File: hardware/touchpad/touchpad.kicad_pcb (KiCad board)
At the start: 2 copper layers, 195.4 x 135.6 mm, 187 parts, among them J1 Conn_01x26_MountingPin, J10 Conn_02x03_Odd_Even, J100 Conn_02x03_Odd_Even, J101 Conn_02x03_Odd_Even, J102 Conn_02x03_Odd_Even, J103 Conn_02x03_Odd_Even, J104 Conn_02x03_Odd_Even, J105 Conn_02x03_Odd_Even, J106 Conn_02x03_Odd_Even, J107 Conn_02x03_Odd_Even, J108 Conn_02x03_Odd_Even, J109 Conn_02x03_Odd_Even, J11 Conn_02x03_Odd_Even, J110 Conn_02x03_Odd_Even, J111 Conn_02x03_Odd_Even, J112 Conn_02x03_Odd_Even, J113 Conn_02x03_Odd_Even, J114 Conn_02x03_Odd_Even, J115 Conn_02x03_Odd_Even, J116 Conn_02x03_Odd_Even, J117 Conn_02x03_Odd_Even, J118 Conn_02x03_Odd_Even, J119 Conn_02x03_Odd_Even, J12 Conn_02x03_Odd_Even, J120 Conn_02x03_Odd_Even, J121 Conn_02x03_Odd_Even, J122 Conn_02x03_Odd_Even, J123 Conn_02x03_Odd_Even, J124 Conn_02x03_Odd_Even, J125 Conn_02x03_Odd_Even, J126 Conn_02x03_Odd_Even, J127 Conn_02x03_Odd_Even, J128 Conn_02x03_Odd_Even, J129 Conn_02x03_Odd_Even, J13 Conn_02x03_Odd_Even, J130 Conn_02x03_Odd_Even, J131 Conn_02x03_Odd_Even, J132 Conn_02x03_Odd_Even, J133 Conn_02x03_Odd_Even, J134 Conn_02x03_Odd_Even, J135 Conn_02x03_Odd_Even, J136 Conn_02x03_Odd_Even, J137 Conn_02x03_Odd_Even, J138 Conn_02x03_Odd_Even, J139 Conn_02x03_Odd_Even, J14 Conn_02x03_Odd_Even, J140 Conn_02x03_Odd_Even, J141 Conn_02x03_Odd_Even, J142 Conn_02x03_Odd_Even, J143 Conn_02x03_Odd_Even, J144 Conn_02x03_Odd_Even, J145 Conn_02x03_Odd_Even, J146 Conn_02x03_Odd_Even, J147 Conn_02x03_Odd_Even, J148 Conn_02x03_Odd_Even, J149 Conn_02x03_Odd_Even, J15 Conn_02x03_Odd_Even, J150 Conn_02x03_Odd_Even, J151 Conn_02x03_Odd_Even, J152 Conn_02x03_Odd_Even, J153 Conn_02x03_Odd_Even, J154 Conn_02x03_Odd_Even, J155 Conn_02x03_Odd_Even, J156 Conn_02x03_Odd_Even, J157 Conn_02x03_Odd_Even, J158 Conn_02x03_Odd_Even, J159 Conn_02x03_Odd_Even, J16 Conn_02x03_Odd_Even, J160 Conn_02x03_Odd_Even, J161 Conn_02x03_Odd_Even, J162 Conn_02x03_Odd_Even, J163 Conn_02x03_Odd_Even, J164 Conn_02x03_Odd_Even, J165 Conn_02x03_Odd_Even, J166 Conn_02x03_Odd_Even, J167 Conn_02x03_Odd_Even, J168 Conn_02x03_Odd_Even, J169 Conn_02x03_Odd_Even, J17 Conn_02x03_Odd_Even, J170 Conn_02x03_Odd_Even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

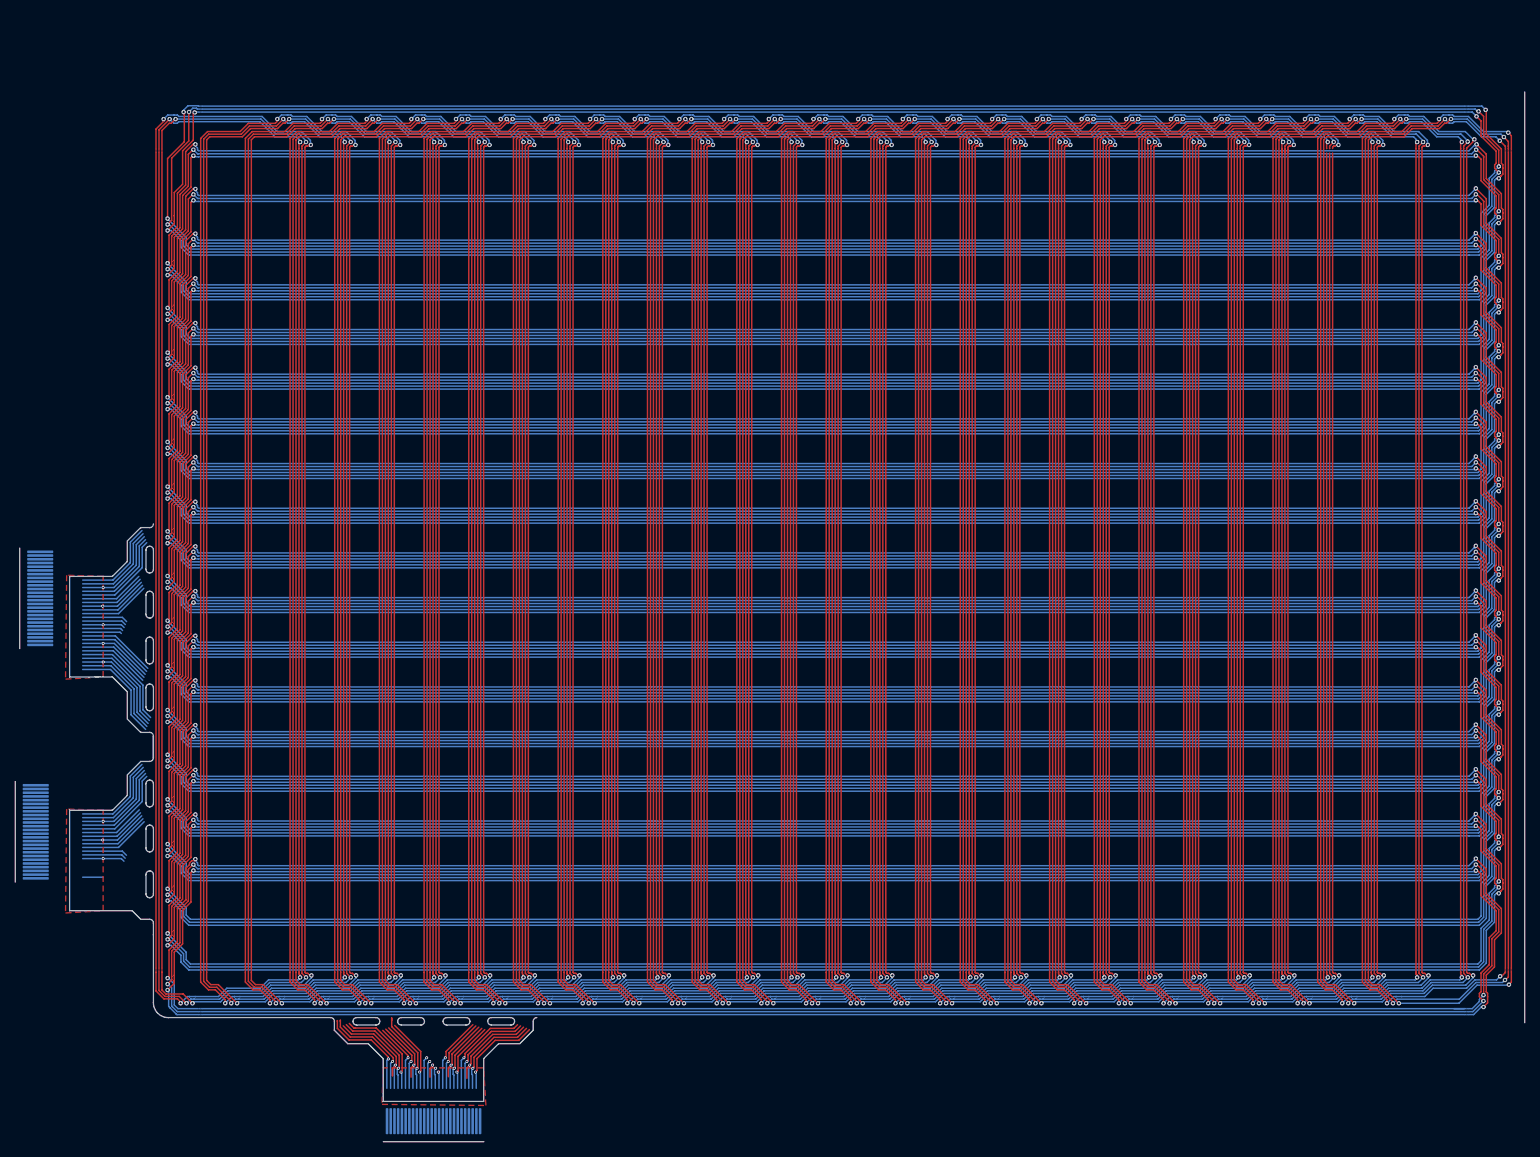
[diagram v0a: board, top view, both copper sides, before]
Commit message: finished touchpad
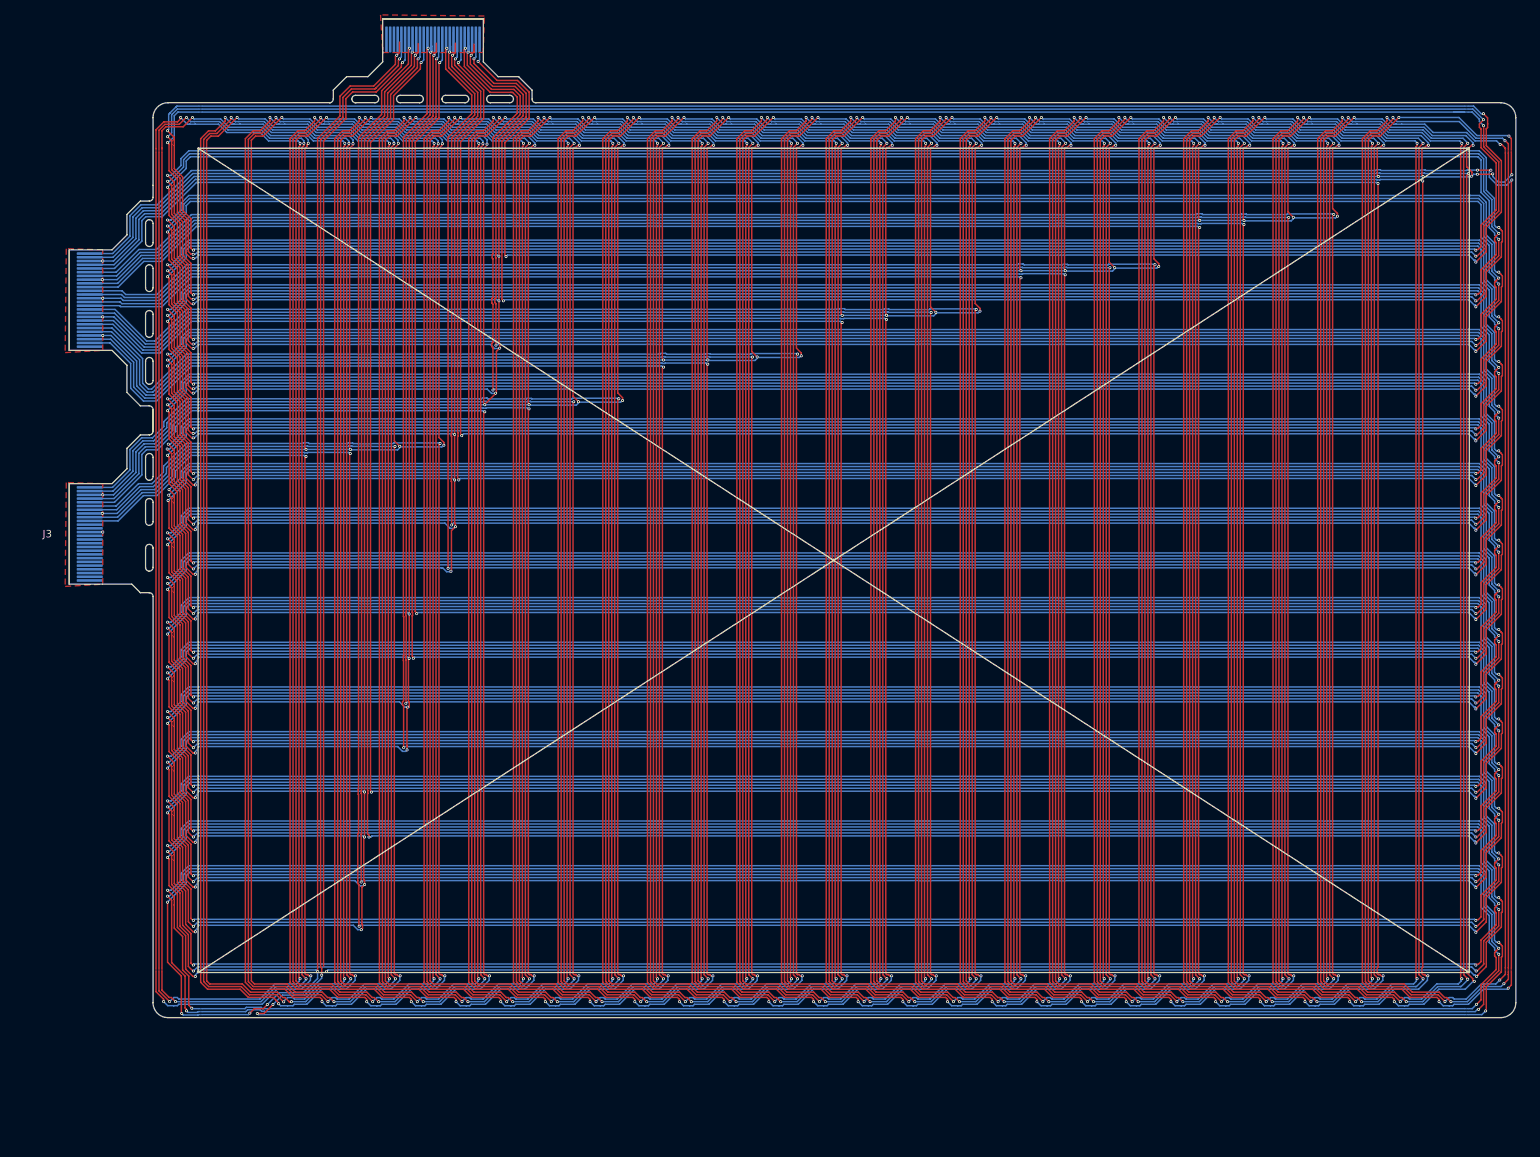
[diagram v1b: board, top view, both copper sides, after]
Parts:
- moved J111 212.0 mm to (72.1, 143.9), turned to -90 degrees
- moved J109 212.0 mm to (72.1, 33.9), turned to -90 degrees
- moved J4 212.0 mm to (253.3, 33.9), turned to -90 degrees
- moved J6 212.0 mm to (253.3, 143.9), turned to -90 degrees
- moved J10 201.8 mm to (247.3, 143.9), turned to -90 degrees
- moved J105 201.8 mm to (78.1, 33.9), turned to -90 degrees
- moved J107 201.8 mm to (78.1, 143.9), turned to -90 degrees
- moved J8 201.8 mm to (247.3, 33.9), turned to -90 degrees
- moved J101 191.9 mm to (84.1, 33.9), turned to -90 degrees
- moved J103 191.9 mm to (84.1, 143.9), turned to -90 degrees
- moved J12 191.9 mm to (241.3, 33.9), turned to -90 degrees
- moved J14 191.9 mm to (241.3, 143.9), turned to -90 degrees
- moved J16 182.2 mm to (235.3, 33.9), turned to -90 degrees
- moved J18 182.2 mm to (235.3, 143.9), turned to -90 degrees
- moved J97 182.2 mm to (90.1, 33.9), turned to -90 degrees
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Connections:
- J3 pad 13: unconnected-(J3-Pin_13-Pad13) -> GND
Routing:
- net Net-(J4-Pin_6): track 3063.2 -> 109.4 mm
- net Net-(J124-Pin_6): track 3049.2 -> 169.4 mm
- net GND: track 51.7 -> 2509.0 mm, vias 0 -> 62
- net /X0: track 0.00 -> 306.2 mm, vias 0 -> 3
- net /Y17: track 13.5 -> 306.4 mm, vias 1 -> 4
- net /X1: track 13.7 -> 299.3 mm, vias 0 -> 1
- net /X2: track 14.2 -> 292.2 mm
- net /X3: track 14.4 -> 285.8 mm, vias 0 -> 1
- net /Y16: track 13.5 -> 284.8 mm, vias 1 -> 2
- net /Y15: track 9.48 -> 271.5 mm, vias 1 -> 2
- net /X4: track 14.6 -> 272.7 mm, vias 0 -> 1
- net /X5: track 9.70 -> 266.1 mm, vias 0 -> 1
- net /Y14: track 9.69 -> 265.4 mm, vias 1 -> 2
- net /X6: track 10.1 -> 259.3 mm
- net /Y13: track 10.0 -> 258.3 mm, vias 1 -> 2
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- added copper zone on F.Cu, net GND
- removed copper zone on F.Cu, net unconnected-(J3-Pin_13-Pad13)
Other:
- board size 195.4 x 135.6 mm -> 194.2 x 134.1 mm

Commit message: started schematics
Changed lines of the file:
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@@
 	)
 	(gr_rect
-		(start 60.05 92.1)
-		(end 64.55 78.6)
+		(start 60.05 78.6)
+		(end 64.55 92.1)
 		(stroke
 			(width 0.15)
@@
 	)
 	(gr_rect
-		(start 115.65 16.2)
-		(end 102.15 20.7)
+		(start 102.15 16.2)
+		(end 115.65 20.7)
 		(stroke
 			(width 0.15)
@@
 	)
 	(gr_rect
-		(start 60.05 60.7)
-		(end 64.55 47.2)
+		(start 60.05 47.2)
+		(end 64.55 60.7)
 		(stroke
 			(width 0.15)
@@
 	)
 	(segment
-		(start 97.601392 32.9)
-		(end 97.601392 33.145997)
+		(start 78.097389 33.569293)
+		(end 78.097389 32.282611)
 		(width 0.2)
 		(layer "F.Cu")
@@
 	)
 	(segment
-		(start 79.871389 31.576)
-		(end 81.797389 29.65)
+		(start 97.601392 32.9)
+		(end 97.601392 33.145997)
 		(width 0.2)
 		(layer "F.Cu")
@@
 	)
 	(segment
-		(start 78.097389 32.375)
-		(end 78.896389 31.576)
+		(start 97.601392 33.145997)
+		(end 97.298096 33.449293)
 		(width 0.2)
 		(layer "F.Cu")
@@
 	)
 	(segment
-		(start 78.097389 33.569293)
-		(end 78.097389 32.375)
+		(start 78.86 31.52)
+		(end 79.9 31.52)
 		(width 0.2)
 		(layer "F.Cu")
@@
 	)
 	(segment
-		(start 97.601392 33.145997)
-		(end 97.298096 33.449293)
+		(start 81.797389 29.622611)
+		(end 81.797389 29.425)
 		(width 0.2)
 		(layer "F.Cu")
@@
 	)
 	(segment
-		(start 81.797389 29.65)
-		(end 81.797389 29.425)
+		(start 79.9 31.52)
+		(end 81.797389 29.622611)
 		(width 0.2)
 		(layer "F.Cu")
@@
 	)
 	(segment
-		(start 78.896389 31.576)
-		(end 79.871389 31.576)
+		(start 78.097389 32.282611)
+		(end 78.86 31.52)
 		(width 0.2)
 		(layer "F.Cu")
@@
 	)
 	(segment
-		(start 96.897389 33.575)
-		(end 96.897389 33.599293)
+		(start 79.73 31.12)
+		(end 78.65 31.12)
 		(width 0.2)
 		(layer "F.Cu")
@@
 	)
 	(segment
-		(start 79.672389 31.225)
-		(end 80.997389 29.9)
+		(start 81.164165 29.427109)
+		(end 81.164165 29.685835)
 		(width 0.2)
 		(layer "F.Cu")
@@
 	)
 	(segment
-		(start 97.047389 33.203612)
-		(end 97.047389 32.824293)
+		(start 96.897389 33.575)
+		(end 96.897389 33.599293)
 		(width 0.2)
 		(layer "F.Cu")
@@
 	)
 	(segment
-		(start 77.697389 33.569293)
-		(end 77.697389 32.275)
+		(start 77.697389 32.072611)
+		(end 77.697389 33.597389)
 		(width 0.2)
 		(layer "F.Cu")
@@
 	)
 	(segment
-		(start 77.697389 32.275)
-		(end 78.747389 31.225)
+		(start 97.047389 33.203612)
+		(end 97.047389 32.824293)
 		(width 0.2)
 		(layer "F.Cu")
@@
 	)
 	(segment
-		(start 77.698096 33.57)
-		(end 77.697389 33.569293)
+		(start 96.898096 33.352905)
+		(end 97.047389 33.203612)
 		(width 0.2)
 		(layer "F.Cu")
@@
 	)
 	(segment
-		(start 96.898096 33.352905)
-		(end 97.047389 33.203612)
+		(start 78.65 31.12)
+		(end 77.697389 32.072611)
 		(width 0.2)
 		(layer "F.Cu")
@@
 	)
 	(segment
-		(start 80.997389 29.9)
-		(end 80.997389 29.425)
+		(start 81.164165 29.685835)
+		(end 79.73 31.12)
 		(width 0.2)
 		(layer "F.Cu")
@@
 	)
 	(segment
-		(start 78.747389 31.225)
-		(end 79.672389 31.225)
+		(start 77.697389 33.597389)
+		(end 77.7 33.6)
 		(width 0.2)
 		(layer "F.Cu")
@@
 	)
 	(via
-		(at 80.997389 29.425)
+		(at 81.164165 29.427109)
 		(size 0.4)
 		(drill 0.2)
@@
 	)
 	(segment
-		(start 82.97201 30.326)
-		(end 86.085613 30.326)
+		(start 82.201 30.325)
+		(end 82.202001 30.326)
 		(width 0.2)
 		(layer "B.Cu")
@@
 	)
 	(segment
-		(start 92.810751 32.566)
-		(end 96.789096 32.566)
+		(start 82.223769 30.327)
+		(end 82.971009 30.327)
 		(width 0.2)
 		(layer "B.Cu")
@@
 	)
 	(segment
-		(start 81.897389 30.325)
-		(end 82.201 30.325)
+		(start 81.164165 29.434165)
+		(end 82.055 30.325)
 		(width 0.2)
 		(layer "B.Cu")
@@
 	)
 	(segment
-		(start 82.222768 30.326)
-		(end 82.223769 30.327)
+		(start 91.691751 31.447)
+		(end 92.810751 32.566)
 		(width 0.2)
 		(layer "B.Cu")
@@
 	)
 	(segment
-		(start 82.201 30.325)
-		(end 82.202001 30.326)
+		(start 86.085613 30.326)
+		(end 87.206613 31.447)
 		(width 0.2)
 		(layer "B.Cu")
@@
 	)
 	(segment
-		(start 82.223769 30.327)
-		(end 82.971009 30.327)
+		(start 82.971009 30.327)
+		(end 82.97201 30.326)
 		(width 0.2)
 		(layer "B.Cu")
@@
 	)
 	(segment
-		(start 82.971009 30.327)
-		(end 82.97201 30.326)
+		(start 82.97201 30.326)
+		(end 86.085613 30.326)
 		(width 0.2)
 		(layer "B.Cu")
@@
 	)
 	(segment
-		(start 91.691751 31.447)
-		(end 92.810751 32.566)
+		(start 82.222768 30.326)
+		(end 82.223769 30.327)
 		(width 0.2)
 		(layer "B.Cu")
@@
 	)
 	(segment
-		(start 80.997389 29.425)
-		(end 81.897389 30.325)
+		(start 81.164165 29.427109)
+		(end 81.164165 29.434165)
 		(width 0.2)
 		(layer "B.Cu")
@@
 	)
 	(segment
-		(start 86.085613 30.326)
-		(end 87.206613 31.447)
+		(start 82.055 30.325)
+		(end 82.201 30.325)
+		(width 0.2)
+		(layer "B.Cu")
+		(net 345)
+	)
+	(segment
+		(start 92.810751 32.566)
+		(end 96.789096 32.566)
 		(width 0.2)
 		(layer "B.Cu")
@@
 	)
 	(segment
-		(start 80.231001 29.975)
-		(end 76.826621 29.975)
-		(width 0.2)
-		(layer "B.Cu")
-		(net 353)
-	)
-	(segment
-		(start 76.368157 29.975)
-		(end 76.347389 29.975)
-		(width 0.2)
-		(layer "B.Cu")
-		(net 353)
-	)
-	(segment
-		(start 91.217328 32.215)
-		(end 86.95614 32.215)
-		(width 0.2)
-		(layer "B.Cu")
-		(net 353)
-	)
-	(segment
 		(start 91.55 32.9)
 		(end 91.55 32.547672)
@@
 	)
 	(segment
-		(start 76.825621 29.976)
-		(end 76.369157 29.976)
-		(width 0.2)
-		(layer "B.Cu")
-		(net 353)
-	)
-	(segment
 		(start 86.95614 32.215)
 		(end 85.83714 31.096)
@@
 	)
 	(segment
-		(start 76.826621 29.975)
-		(end 76.825621 29.976)
+		(start 76.292389 29.92)
+		(end 75.797389 29.425)
 		(width 0.2)
 		(layer "B.Cu")
@@
 	)
 	(segment
-		(start 76.369157 29.976)
-		(end 76.368157 29.975)
+		(start 91.217328 32.215)
+		(end 86.95614 32.215)
 		(width 0.2)
 		(layer "B.Cu")
@@
 	)
 	(segment
-		(start 76.347389 29.975)
-		(end 75.797389 29.425)
+		(start 85.83714 31.096)
+		(end 81.436 31.096)
 		(width 0.2)
 		(layer "B.Cu")
@@
 	)
 	(segment
-		(start 81.352001 31.096)
-		(end 80.231001 29.975)
+		(start 81.436 31.096)
+		(end 80.26 29.92)
 		(width 0.2)
 		(layer "B.Cu")
@@
 	)
 	(segment
-		(start 85.83714 31.096)
-		(end 81.352001 31.096)
+		(start 80.26 29.92)
+		(end 76.292389 29.92)
 		(width 0.2)
 		(layer "B.Cu")
@@
 	)
 	(segment
-		(start 76.625959 29.425)
-		(end 76.597389 29.425)
+		(start 92.15 32.423379)
+		(end 91.582328 31.855707)
 		(width 0.2)
 		(layer "B.Cu")
@@
 	)
 	(segment
-		(start 85.982529 30.745)
-		(end 81.497389 30.745)
+		(start 80.42028 29.51)
+		(end 76.682389 29.51)
 		(width 0.2)
 		(layer "B.Cu")
@@
 	)
 	(segment
-		(start 92.15 32.423379)
-		(end 91.582328 31.855707)
+		(start 76.682389 29.51)
+		(end 76.597389 29.425)
 		(width 0.2)
 		(layer "B.Cu")
@@
 	)
 	(segment
-		(start 76.796389 29.624)
+		(start 76.625959 29.425)
 		(end 76.597389 29.425)
 		(width 0.2)
@@
 	)
 	(segment
-		(start 91.582328 31.855707)
-		(end 87.093236 31.855707)
+		(start 92.15 32.9)
+		(end 92.15 32.423379)
 		(width 0.2)
 		(layer "B.Cu")
@@
 	)
 	(segment
-		(start 80.376389 29.624)
-		(end 76.796389 29.624)
+		(start 81.65528 30.745)
+		(end 80.42028 29.51)
 		(width 0.2)
 		(layer "B.Cu")
@@
 	)
 	(segment
-		(start 81.497389 30.745)
-		(end 80.376389 29.624)
+		(start 87.093236 31.855707)
+		(end 85.982529 30.745)
 		(width 0.2)
 		(layer "B.Cu")
@@
 	)
 	(segment
-		(start 92.15 32.9)
-		(end 92.15 32.423379)
+		(start 91.582328 31.855707)
+		(end 87.093236 31.855707)
 		(width 0.2)
 		(layer "B.Cu")
@@
 	)
 	(segment
-		(start 87.093236 31.855707)
-		(end 85.982529 30.745)
+		(start 85.982529 30.745)
+		(end 81.65528 30.745)
 		(width 0.2)
 		(layer "B.Cu")

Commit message: fixed stuff
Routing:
- net /Y16: track 284.8 -> 127.6 mm, vias 2 -> 1
- net Net-(J105-Pin_6): track 109.4 -> 0.00 mm
- net GND: track 2509.0 -> 2419.2 mm, vias 62 -> 56
- net /Y17: track 306.4 -> 293.7 mm, vias 4 -> 2
- net /X0: track 306.2 -> 296.6 mm, vias 3 -> 0
- net /X23: track 135.9 -> 128.8 mm
- net /X22: track 142.2 -> 135.1 mm
- net /X7: track 253.0 -> 246.3 mm
- net /X18: track 172.4 -> 165.7 mm
- net /X19: track 166.0 -> 159.3 mm
- net /X6: track 259.3 -> 252.6 mm
- net /X5: track 266.1 -> 259.5 mm
- net /X4: track 272.7 -> 266.1 mm
- net /X2: track 292.2 -> 285.6 mm
- net /X3: track 285.8 -> 279.3 mm
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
